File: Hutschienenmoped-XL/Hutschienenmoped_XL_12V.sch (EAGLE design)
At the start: 138 parts, among them J1 638207222005, J13 638207222005, J15 638207222008, J2 645004114822, J4 61300421121, J7 638207222005, J8 638207222007, U4 TLE9250VSJ

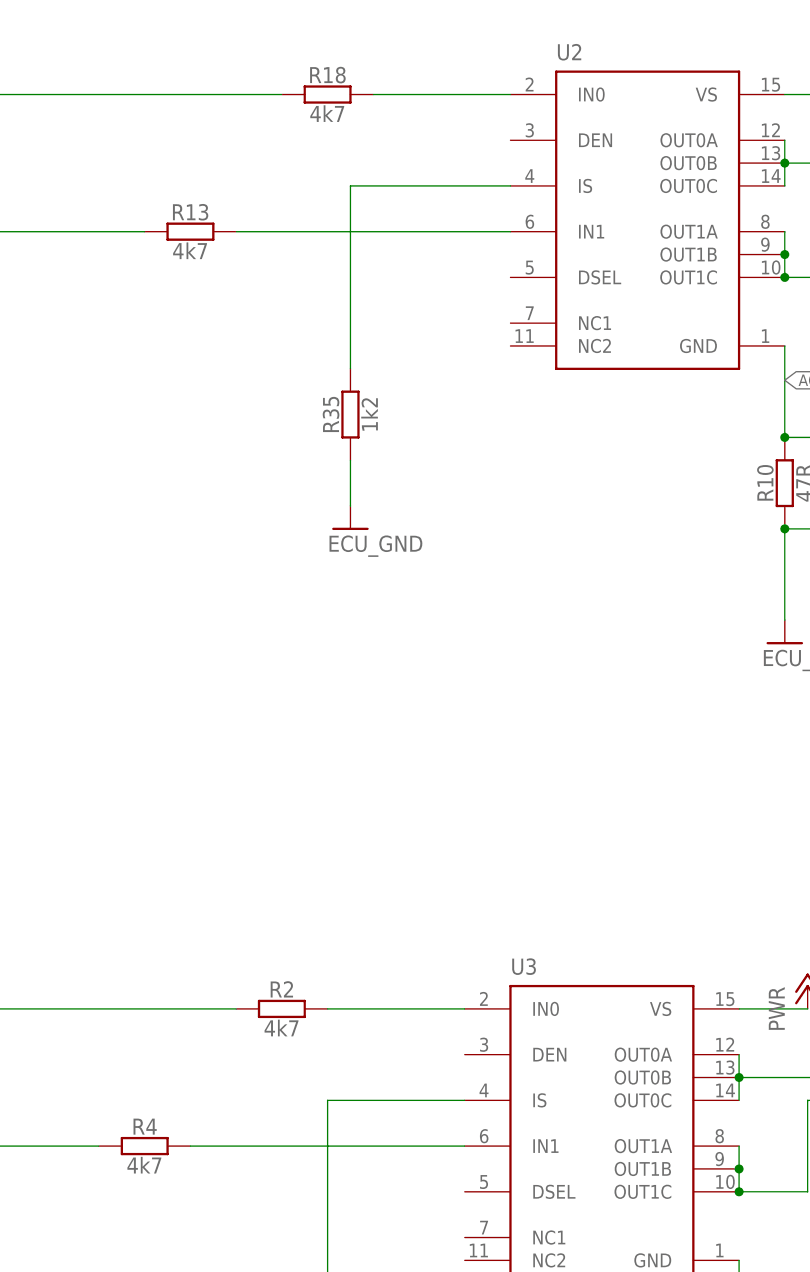
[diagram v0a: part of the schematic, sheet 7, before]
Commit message: Change font setting to not always vector, adjust capacitor element attributes. Update diode elements' positions and attributes.
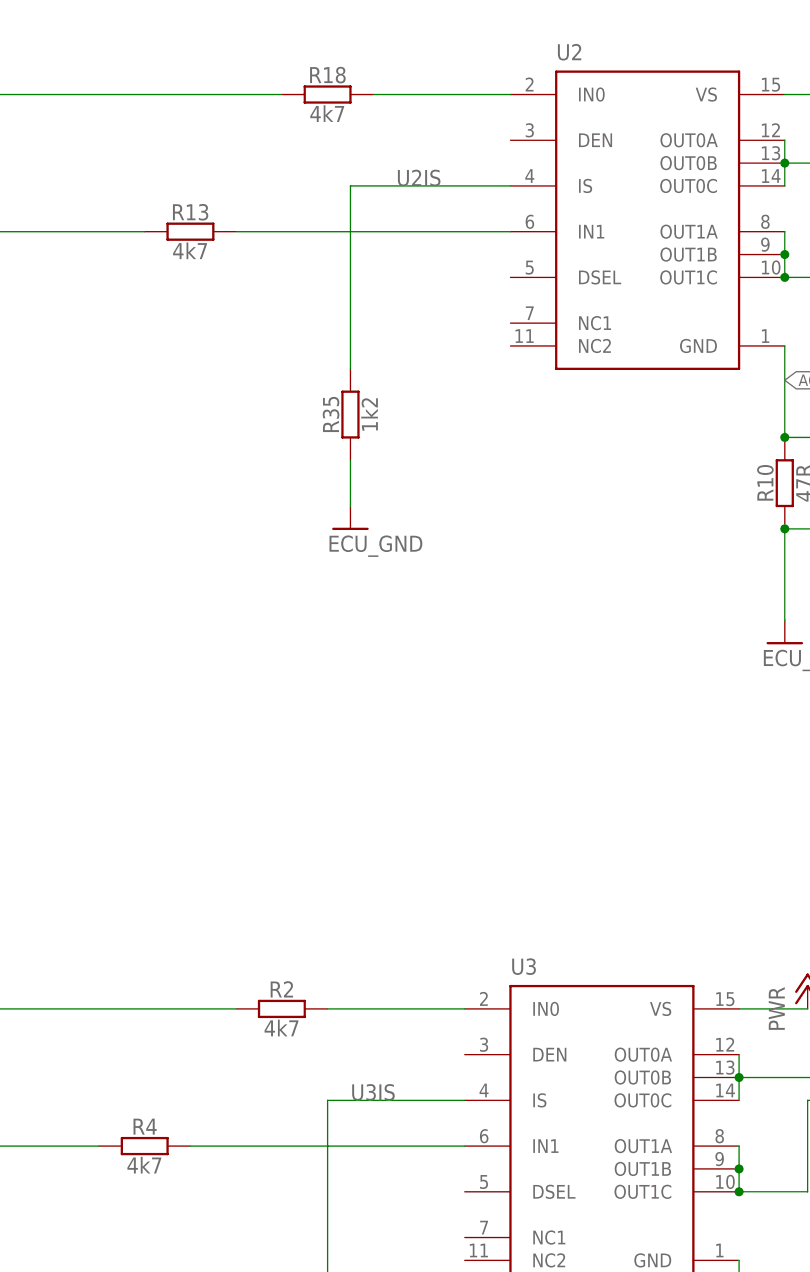
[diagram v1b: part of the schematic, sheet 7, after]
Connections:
- net N$16 renamed U6IS
- net N$20 renamed U2IS
- net N$21 renamed U3IS
- net N$7 renamed U5IS
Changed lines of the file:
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@@
 </segment>
 </net>
-<net name="N$20" class="0">
+<net name="U2IS" class="0">
 <segment>
 <pinref part="R35" gate="G$1" pin="2"/>
@@
 <wire x1="43.18" y1="99.06" x2="43.18" y2="119.38" width="0.1524" layer="91"/>
 <wire x1="43.18" y1="119.38" x2="60.96" y2="119.38" width="0.1524" layer="91"/>
-</segment>
-</net>
-<net name="N$21" class="0">
+<label x="48.26" y="119.38" size="1.778" layer="95"/>
+</segment>
+</net>
+<net name="U3IS" class="0">
 <segment>
 <pinref part="R36" gate="G$1" pin="2"/>
@@
 <wire x1="40.64" y1="-5.08" x2="40.64" y2="17.78" width="0.1524" layer="91"/>
 <wire x1="40.64" y1="17.78" x2="55.88" y2="17.78" width="0.1524" layer="91"/>
+<label x="43.18" y="17.78" size="1.778" layer="95"/>
 </segment>
 </net>
@@
 </segment>
 </net>
-<net name="N$7" class="0">
+<net name="U5IS" class="0">
 <segment>
 <pinref part="R37" gate="G$1" pin="2"/>
@@
 <wire x1="48.26" y1="99.06" x2="48.26" y2="119.38" width="0.1524" layer="91"/>
 <wire x1="48.26" y1="119.38" x2="60.96" y2="119.38" width="0.1524" layer="91"/>
-</segment>
-</net>
-<net name="N$16" class="0">
+<label x="50.8" y="119.38" size="1.778" layer="95"/>
+</segment>
+</net>
+<net name="U6IS" class="0">
 <segment>
 <pinref part="R38" gate="G$1" pin="2"/>
@@
 <wire x1="40.64" y1="-5.08" x2="40.64" y2="17.78" width="0.1524" layer="91"/>
 <wire x1="40.64" y1="17.78" x2="55.88" y2="17.78" width="0.1524" layer="91"/>
-</segment>
-</net>
+<label x="45.72" y="17.78" size="1.778" layer="95"/>
+</segment>
+</net>
